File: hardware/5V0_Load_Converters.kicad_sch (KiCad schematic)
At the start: 73 parts, among them J19 61300311121, Q2 SI2302DDS-T1-GE3, Q26 EPC2016C, Q27 EPC2016C, U30 LTC3833EUDC-TRPBF, U4 INA199C1DCKR

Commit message: commit
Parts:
- removed R30: 5m, symbol Device:R_US
- removed R31, R32: 2.2R, symbol Device:R_US
- removed R40: 100k, symbol Device:R_US
- removed R42, R43, R44, R45, R46: 10R, symbol Device:R_US
- removed R48: 8m, symbol Device:R_US
- removed R49, R51, R53, R55: 0.0R, symbol Device:R_US
- added R30: 5m, footprints:WSL20105L000FEA, symbol WSL20105L000FEA:WSL20105L000FEA
- added R40: 100k, footprints:CRCW0603100KFKEAHP, symbol CRCW0603100KFKEAHP:CRCW0603100KFKEAHP
- added R42, R43, R44, R45, R46: 10R, footprints:CRCW060310R0FKEAHP, symbol CRCW060310R0FKEAHP:CRCW060310R0FKEAHP
- added R48: 8m, footprints:WSL20108L000FEA18, symbol WSL20108L000FEA18:WSL20108L000FEA18
- added R76 (x4): 0.0R, footprints:CRCW06030000Z0EAHP, symbol CRCW06030000Z0EAHP:CRCW06030000Z0EAHP
- added R95 (x2): 2.2R, footprints:CRCW06032R20FKEAHP, symbol CRCW06032R20FKEAHP:CRCW06032R20FKEAHP
- R33, R34, R39: footprint (none) -> footprints:CRCW0603100KFKEAHP; symbol Device:R_US -> CRCW0603100KFKEAHP:CRCW0603100KFKEAHP; Arrow Part Number (none) -> CRCW0603100KFKEAHP; Arrow Price/Stock (none) -> https://www.arrow.com/en/products/crcw0603100kfkeahp/vishay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; Height (none) -> 0.55; Manufacturer_Name (none) -> Vishay; Manufacturer_Part_Number (none) -> CRCW0603100KFKEAHP; Mouser Part Number (none) -> 71-CRCW0603100KFKEAH; Mouser Price/Stock (none) -> https://www.mouser.co.uk/ProductDetail/Vishay-Dale/CRCW0603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
- R41: footprint (none) -> footprints:CRCW060310R0FKEAHP; symbol Device:R_US -> CRCW060310R0FKEAHP:CRCW060310R0FKEAHP; Arrow Part Number (none) -> CRCW060310R0FKEAHP; Arrow Price/Stock (none) -> https://www.arrow.com/en/products/crcw060310r0fkeahp/vishay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; Height (none) -> 0.5; Manufacturer_Name (none) -> Vishay; Manufacturer_Part_Number (none) -> CRCW060310R0FKEAHP; Mouser Part Number (none) -> 71-CRCW060310R0FKEAH; Mouser Price/Stock (none) -> https://www.mouser.co.uk/ProductDetail/Vishay-Dale/CRCW0603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
- R47: footprint (none) -> footprints:WSL20108L000FEA18; symbol Device:R_US -> WSL20108L000FEA18:WSL20108L000FEA18
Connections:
- net 5V0: now also R47.1, R44.1, R46.1, R48.1, R76.1, R76.1; no longer R47.2
- net 5V0_A_~{EN}: now also R34.2; no longer R34.1
- net 5V0_B_~{EN}: now also R33.1; no longer R33.2
- net 5V0_VCC1: now also R39.2; no longer R39.1
- net 5V0_VCC2: now also R40.2
- net GND: now also R34.1; no longer R34.2
- net VBUS: now also R30.1
- net VBUS_BK5V0: now also R33.2, R30.2, R95.2, R95.2; no longer R33.1
- net at C32.2, R50.2, U30.2 (VOSNS+): now also R76.1
- net at R52.1: now also R76.2
- net at L1.2: now also R47.2, R43.1; no longer R47.1
- net at L2.2: now also R45.1, R48.2
- net at C11.2, U30.10 (VIN): now also R95.1
- net at U30.16 (BOOST): now also R42.2
- net at U30.17 (PGOOD): now also R40.1
- net at C19.1, U30.18 (SENSE+): now also R45.2
- net at C19.2, U30.19 (SENSE-): now also R46.2
- net at C33.2, R54.2, U30.2 (VOSNS+): now also R76.1
- net at C10.2, U30.10 (VIN): now also R95.1
- net at C18.2, U30.19 (SENSE-): now also R44.2
- net at C18.1, U30.18 (SENSE+): now also R43.2
- net at R56.1: now also R76.2
- net at R50.1: now also R76.2
- net at U30.17 (PGOOD): now also R39.1; no longer R39.2
- net at C21.1, D13.1 (K): now also R42.1
- net at R54.1: now also R76.2
- net at C20.1, D13.1 (K): now also R41.1; no longer R41.2
- net at U30.16 (BOOST): now also R41.2; no longer R41.1
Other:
- moved on the sheet: R33, R34, R39, R41, R47

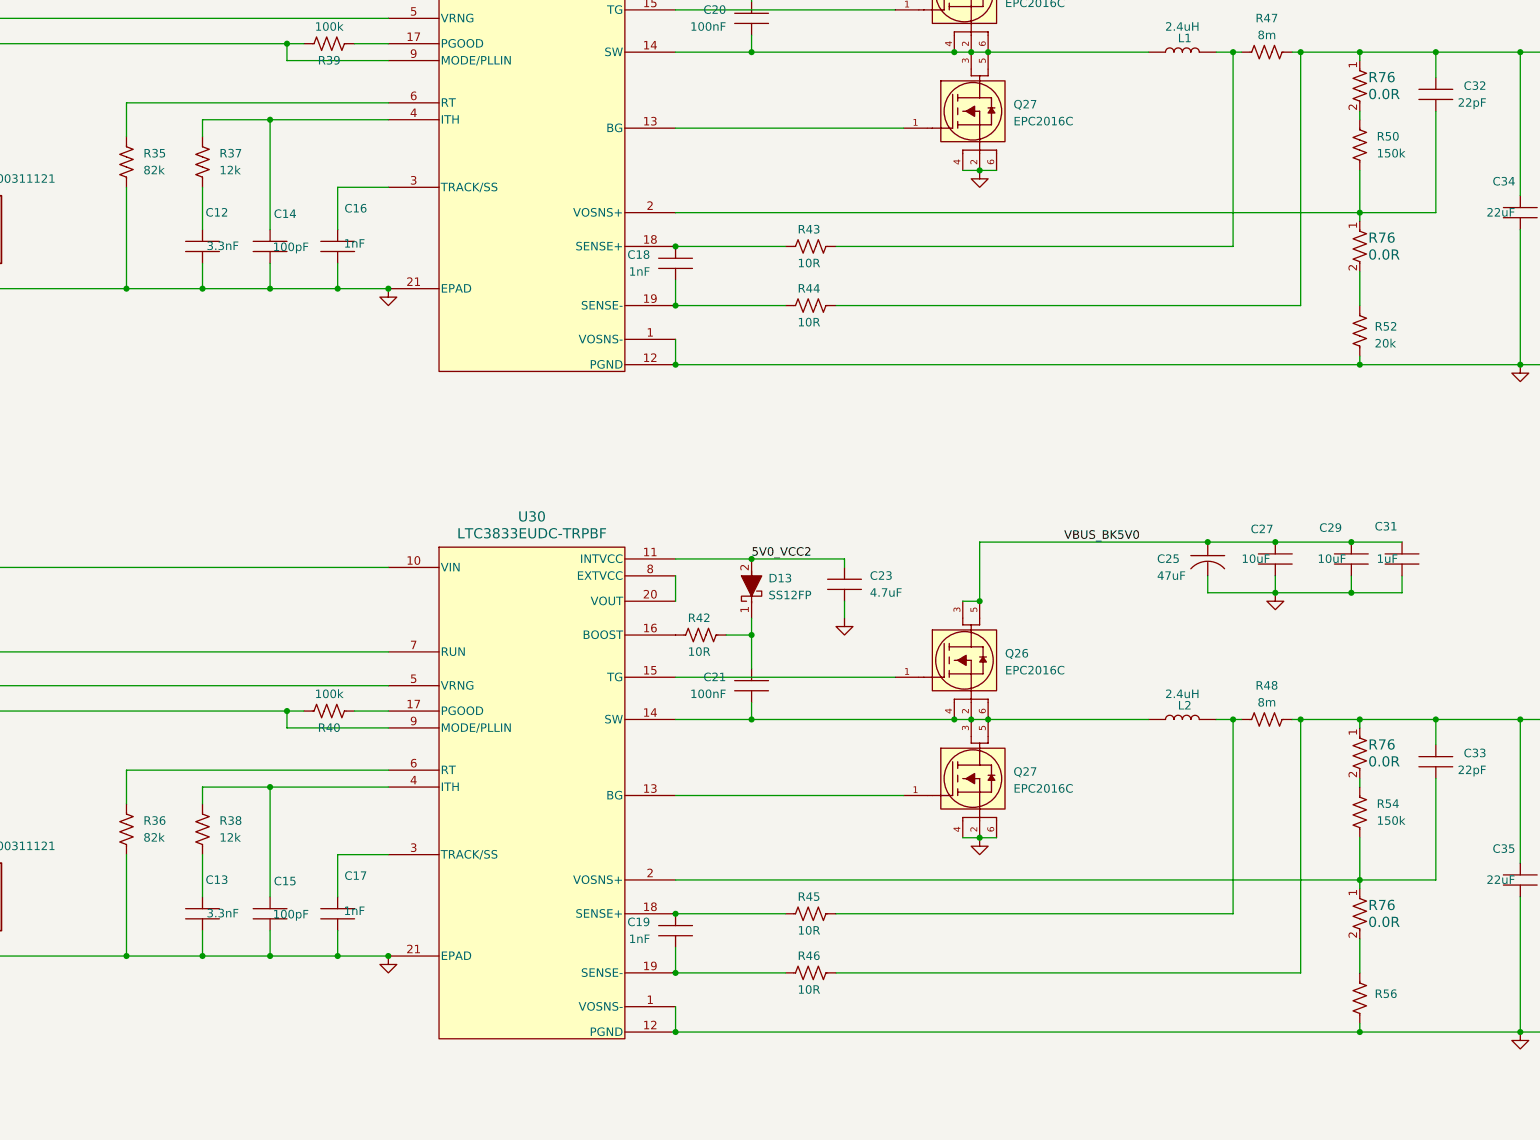
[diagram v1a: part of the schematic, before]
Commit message: hardware: update in footprints
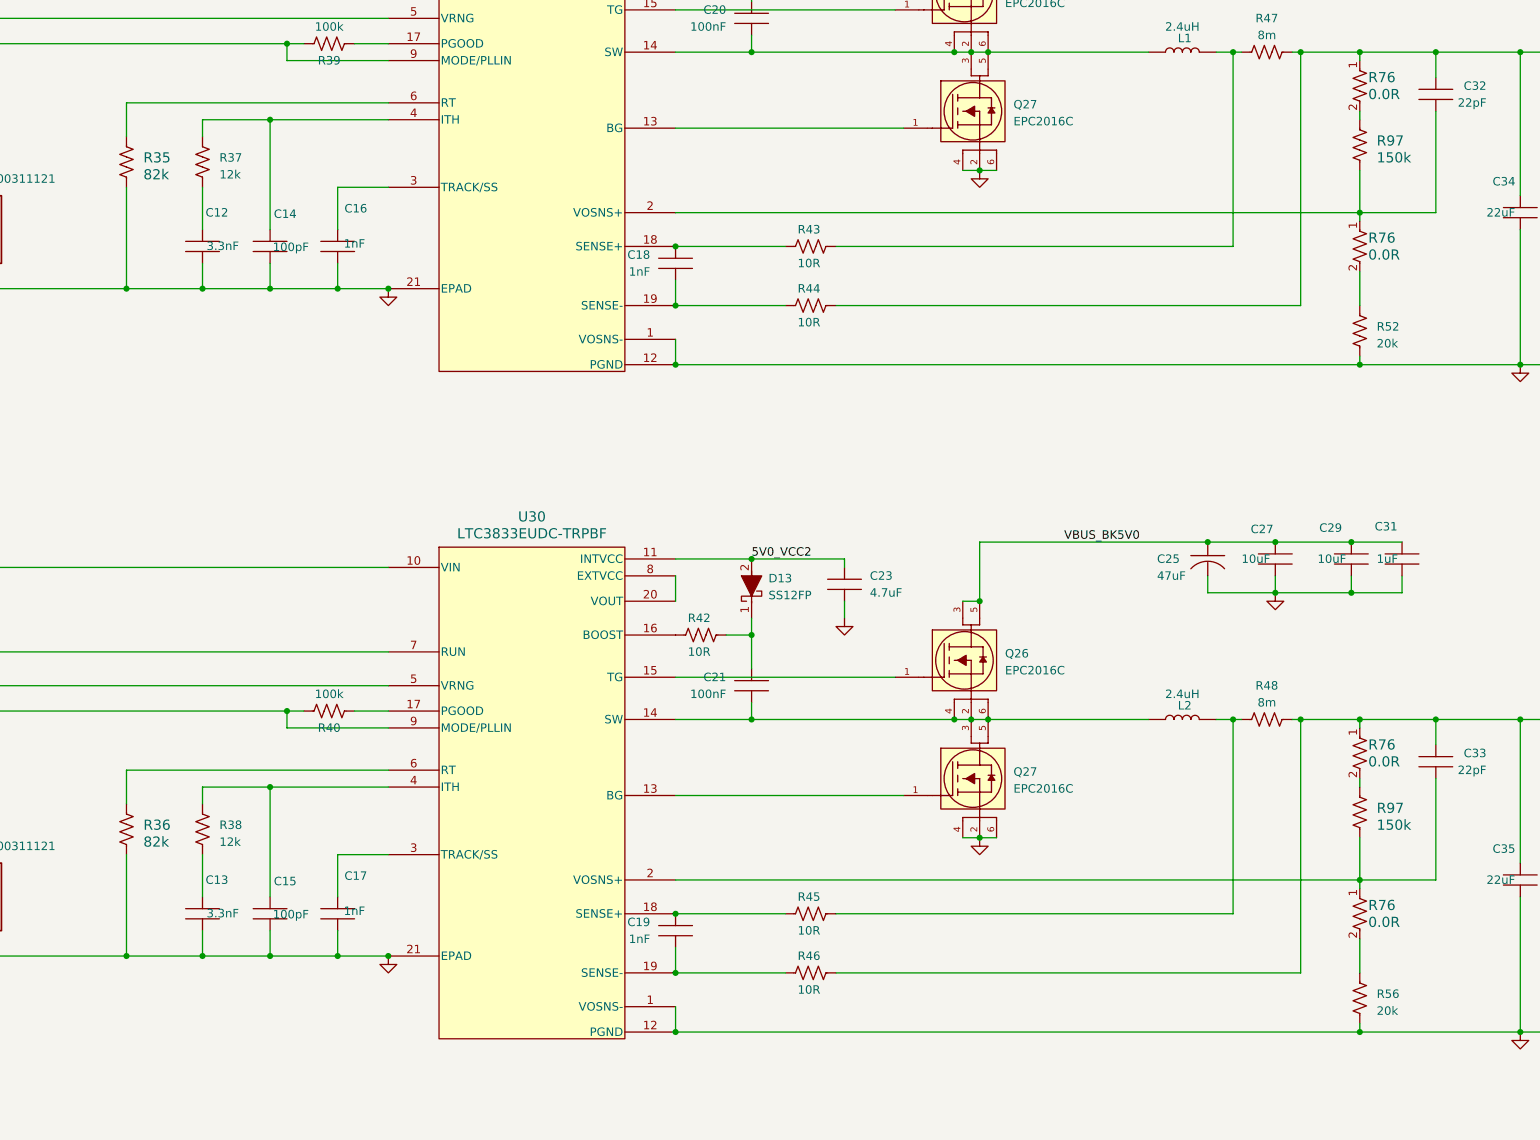
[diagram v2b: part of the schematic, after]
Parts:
- removed R35, R36: 82k, symbol Device:R_US
- removed R50, R54: 150k, symbol Device:R_US
- removed R56: 20k, symbol Device:R_US
- added R35, R36: 82k, footprints:CRCW060382K0FKEA, symbol CRCW060382K0FKEA:CRCW060382K0FKEA
- added R56: 20k, footprints:CRCW060320K0FKEAHP, symbol CRCW060320K0FKEAHP:CRCW060320K0FKEAHP
- added R97 (x2): 150k, footprints:CRCW0603150KFKEAHP, symbol CRCW0603150KFKEAHP:CRCW0603150KFKEAHP
- R37, R38: footprint (none) -> footprints:CRCW060312K0FKEAHP; symbol Device:R_US -> CRCW060312K0FKEAHP:CRCW060312K0FKEAHP; automotive (none) -> Yes; automotive grade (none) -> Grade 0; category (none) -> Res; composition (none) -> Thick Film; device class L1 (none) -> Passive Components; device class L2 (none) -> Resistors; device class L3 (none) -> Chip SMD Resistors; height (none) -> 0.55mm; ipc land pattern name (none) -> RESC16085X45; lead free (none) -> Yes; library id (none) -> e050c09dfdbc8558; manufacturer (none) -> Vishay; package (none) -> 0603; power (none) -> 250mW; power rating (none) -> 0.33W; resistance (none) -> 12kΩ; rohs (none) -> Yes; series (none) -> CRCW-HP e3; temperature coefficient (none) -> 100ppm/°C; temperature range high (none) -> +155°C; temperature range low (none) -> -55°C; tolerance (none) -> 1%; voltage rating (none) -> 75V
- R52: footprint (none) -> footprints:CRCW060320K0FKEAHP; symbol Device:R_US -> CRCW060320K0FKEAHP:CRCW060320K0FKEAHP; automotive (none) -> Yes; automotive grade (none) -> Grade 0; category (none) -> Res; composition (none) -> Thick Film; device class L1 (none) -> Passive Components; device class L2 (none) -> Resistors; device class L3 (none) -> Chip SMD Resistors; height (none) -> 0.55mm; ipc land pattern name (none) -> RESC16085X45; lead free (none) -> Yes; library id (none) -> 6d0e00b833a89e4b; manufacturer (none) -> Vishay; package (none) -> 0603; power (none) -> 250mW; power rating (none) -> 0.33W; resistance (none) -> 20kΩ; rohs (none) -> Yes; series (none) -> CRCW-HP e3; temperature coefficient (none) -> 100ppm/°C; temperature range high (none) -> +155°C; temperature range low (none) -> -55°C; tolerance (none) -> 1%; voltage rating (none) -> 75V
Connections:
- net GND: now also R52.1, R35.1, R36.1, R56.1; no longer R52.2
- net at C33.2, R76.1, U30.2 (VOSNS+): now also R97.1
- net at C15.1, U30.4 (ITH): now also R38.2; no longer R38.1
- net at U30.6 (RT): now also R36.2
- net at R76.2: now also R52.2; no longer R52.1
- net at R76.2: now also R56.2
- net at R76.2: now also R97.2 (x2)
- net at C32.2, R76.1, U30.2 (VOSNS+): now also R97.1
- net at C13.1: now also R38.1; no longer R38.2
- net at C14.1, U30.4 (ITH): now also R37.2; no longer R37.1
- net at U30.6 (RT): now also R35.2
- net at C12.1: now also R37.1; no longer R37.2
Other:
- moved on the sheet: R37, R38, R52

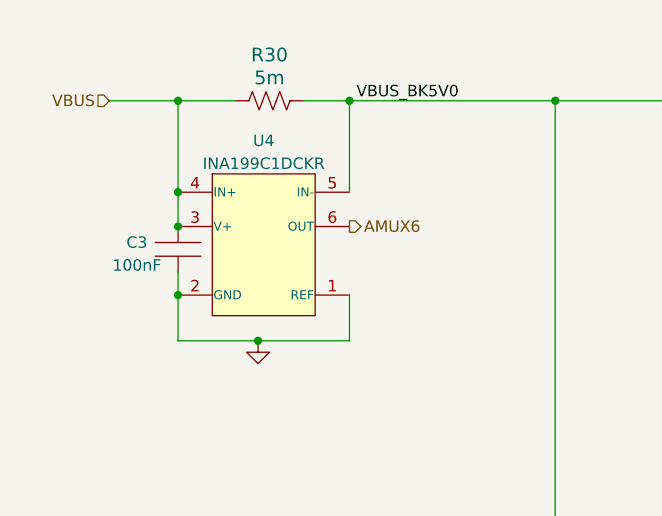
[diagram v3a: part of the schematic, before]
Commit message: hardware: Updating some footprints and 3D models.
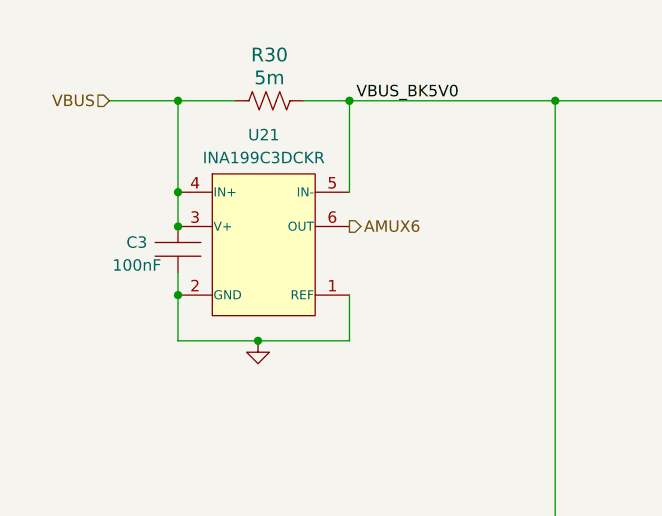
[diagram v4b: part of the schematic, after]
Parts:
- removed U4: INA199C1DCKR, footprints:INA199C1DCKR, symbol INA199C1DCKR:INA199xxDCK
- added U21: INA199C3DCKR, Package_TO_SOT_SMD:SOT-363_SC-70-6, symbol INA199C3DCKR:INA199xxDCK
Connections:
- net AMUX6: now also U21.6 (OUT)
- net GND: now also U21.1 (REF), U21.2 (GND)
- net VBUS: now also U21.3 (V+), U21.4 (IN+)
- net VBUS_BK5V0: now also U21.5 (IN-)
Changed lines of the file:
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@@
   (junction (at 33.02 25.4) (diameter 0) (color 0 0 0 0)
   )
+  (junction (at 33.02 39.37) (diameter 0) (color 0 0 0 0)
+  )
   (junction (at 372.11 195.58) (diameter 0) (color 0 0 0 0)
   )
@@
   (junction (at 74.93 125.73) (diameter 0) (color 0 0 0 0)
   )
-  (junction (at 33.02 35.56) (diameter 0) (color 0 0 0 0)
-  )
   (junction (at 118.11 25.4) (diameter 0) (color 0 0 0 0)
   )
@@
   (junction (at 381 148.59) (diameter 0) (color 0 0 0 0)
   )
-  (junction (at 33.02 46.99) (diameter 0) (color 0 0 0 0)
-  )
   (junction (at 245.11 186.69) (diameter 0) (color 0 0 0 0)
   )
@@
   (junction (at 339.09 48.26) (diameter 0) (color 0 0 0 0)
   )
+  (junction (at 33.02 35.56) (diameter 0) (color 0 0 0 0)
+  )
   (junction (at 359.41 48.26) (diameter 0) (color 0 0 0 0)
   )
@@
   (junction (at 339.09 148.59) (diameter 0) (color 0 0 0 0)
   )
-  (junction (at 33.02 39.37) (diameter 0) (color 0 0 0 0)
-  )
   (junction (at 201.93 83.82) (diameter 0) (color 0 0 0 0)
   )
@@
   (junction (at 347.98 72.39) (diameter 0) (color 0 0 0 0)
   )
+  (junction (at 33.02 46.99) (diameter 0) (color 0 0 0 0)
+  )
   (junction (at 162.56 184.15) (diameter 0) (color 0 0 0 0)
   )
@@
     (stroke (width 0) (type default))
   )
+  (wire (pts (xy 33.02 35.56) (xy 33.02 39.37))
+    (stroke (width 0) (type default))
+  )
   (wire (pts (xy 194.31 180.34) (xy 194.31 184.15))
     (stroke (width 0) (type default))
@@
     (stroke (width 0) (type default))
   )
-  (wire (pts (xy 33.02 25.4) (xy 33.02 35.56))
-    (stroke (width 0) (type default))
-  )
   (wire (pts (xy 245.11 191.77) (xy 245.11 195.58))
     (stroke (width 0) (type default))
@@
     (stroke (width 0) (type default))
   )
-  (wire (pts (xy 33.02 35.56) (xy 33.02 39.37))
+  (wire (pts (xy 33.02 25.4) (xy 33.02 35.56))
     (stroke (width 0) (type default))
   )
@@
     (stroke (width 0) (type default))
   )
+  (wire (pts (xy 33.02 46.99) (xy 33.02 52.07))
+    (stroke (width 0) (type default))
+  )
   (wire (pts (xy 328.93 77.47) (xy 328.93 48.26))
     (stroke (width 0) (type default))
@@
     (stroke (width 0) (type default))
   )
-  (wire (pts (xy 33.02 52.07) (xy 33.02 46.99))
+  (wire (pts (xy 33.02 44.45) (xy 33.02 46.99))
     (stroke (width 0) (type default))
   )
@@
     (stroke (width 0) (type default))
   )
-  (wire (pts (xy 33.02 44.45) (xy 33.02 46.99))
-    (stroke (width 0) (type default))
-  )
   (wire (pts (xy 173.99 80.01) (xy 173.99 83.82))
     (stroke (width 0) (type default))
@@
     )
   )
+  (symbol (lib_id "INA199C3DCKR:INA199xxDCK") (at 20.32 54.61 0) (unit 1)
+    (in_bom yes) (on_board yes) (dnp no) (fields_autoplaced)
+    (property "Reference" "U21" (at 42.545 29.21 0)
+      (effects (font (size 1.27 1.27)))
+    )
+    (property "Value" "INA199C3DCKR" (at 42.545 31.75 0)
+      (effects (font (size 1.27 1.27)))
+    )
+    (property "Footprint" "Package_TO_SOT_SMD:SOT-363_SC-70-6" (at 43.942 53.848 0)
+      (effects (font (size 1.27 1.27)) hide)
+    )
+    (property "Datasheet" "http://www.ti.com/lit/ds/symlink/ina199.pdf" (at 42.926 56.134 0)
+      (effects (font (size 1.27 1.27)) hide)
+    )
+    (pin "1")
+    (pin "2")
+    (pin "3")
+    (pin "4")
+    (pin "5")
+    (pin "6")
+    (instances
+      (project "eps-re_project"
+        (path "/2eebaa11-d7ed-4bfd-bc8e-988f68654d29/6f34948c-43a8-4614-b8ed-90c5b6b9b243"
+          (reference "U21") (unit 1)
+        )
+        (path "/2eebaa11-d7ed-4bfd-bc8e-988f68654d29/6cd5fe02-9b19-49bf-9109-b0a2c2f10c14"
+          (reference "U22") (unit 1)
+        )
+      )
+    )
+  )
   (symbol (lib_id "LTC3833EUDC#TRPBF:LTC3833EUDC-TRPBF") (at 196.85 128.27 0) (unit 1)
     (in_bom yes) (on_board yes) (dnp no) (fields_autoplaced)
@@
         )
       )
-    )
-  )
-  (symbol (lib_id "INA199C1DCKR:INA199xxDCK") (at 20.32 54.61 0) (unit 1)
-    (in_bom yes) (on_board yes) (dnp no)
-    (property "Reference" "U4" (at 42.545 29.845 0)
-      (effects (font (size 1.27 1.27)))
-    )
-    (property "Value" "INA199C1DCKR" (at 42.545 32.385 0)
-      (effects (font (size 1.27 1.27)))
-    )
-    (property "Footprint" "footprints:INA199C1DCKR " (at 43.942 53.848 0)
-      (effects (font (size 1.27 1.27)) hide)
-    )
-    (property "Datasheet" "http://www.ti.com/lit/ds/symlink/ina199.pdf" (at 42.926 56.134 0)
-      (effects (font (size 1.27 1.27)) hide)
-    )
-    (pin "1")
-    (pin "2")
-    (pin "3")
-    (pin "4")
-    (pin "5")
-    (pin "6")
-    (instances
-      (project "eps-re_project"
-        (path "/2eebaa11-d7ed-4bfd-bc8e-988f68654d29/b2d6a676-b7d9-423e-8a54-05279452700b"
-          (reference "U4") (unit 1)
-        )
-        (path "/2eebaa11-d7ed-4bfd-bc8e-988f68654d29/4f028e55-4c46-47b6-9c45-f6b50d9d4db8"
-          (reference "U14") (unit 1)
-        )
-        (path "/2eebaa11-d7ed-4bfd-bc8e-988f68654d29/6cd5fe02-9b19-49bf-9109-b0a2c2f10c14"
-          (reference "U22") (unit 1)
-        )
-      )
-      (project "EPS Analogico"
-        (path "/9af6272d-3cb8-4e37-b792-5888e300588f"
-          (reference "U1") (unit 1)
-        )
-      )
